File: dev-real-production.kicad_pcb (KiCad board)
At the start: 4 copper layers, 105 x 105 mm, 320 parts, among them IC1 ICM-42670-P, IC2 ENS161-BLGT_LGA9_T&R_1k5, J1 VIN_IN, J10 USB-C USB2 DEBUG, J11 ARM_JTAG_10, J12 SOP0_SELECT, J13 SOP1_SELECT, J14 Conn_01x03, J15 Conn_01x03, J16 ARM_JTAG_10, J17 USB-C Receptacle USB2, J18 Conn_01x03_Pin, J19 Cortex SWD/JTAG, J2 TP_EN_PG, J20 USB-C USB2 DEVICE, J21 HR911105A MAGJACK, J22 Conn_02x10_Counter_Clockwise, J23 Conn_02x04_Odd_Even, J3 TP_SW_FB, J4 USB-C Receptacle USB2, J5 Conn_01x03_Pin, J6 ARM_Cortex_Debug_10, J7 SMA_ANT_50OHM, J8 3V3_IN, U1 MMC5633NJL, U10 USBLC6-2P6, U11 FT230XS-R, U12 FT230XS-R, U13 IWRL6432BDBAAMFR, U14 MX25R1635FZUIH0, U15 MX25R1635FZUIH0, U16 AMS1117-1.8, U17 THS8136, U18 MM8108-MF15457, U19 AP2112K-1.8, U2 LPS22HH, U20 PGA113AIDGSR, U21 AD9609BCPZRL7-80, U22 MCP6D11T-E/MS, U23 STM32H7S3Z8T6, U24 LAN8742A-CZ-TR, U25 USBLC6-2SC6, U3 MIC28516T-E/PHA, U4 RP2350B, U5 XCC1352R1F3RGZR, U6 XMSSJJ3G0PA-054, U7 TLV75518PDBV, U8 TLV75518PDBVR, U9 USBLC6-2P6, Y1 12MHz ABM8-272-T3, Y2 48MHz, Y3 40MHz, Y4 40MHz, Y5 24MHz, Y6 32.768kHz, Y7 25MHz

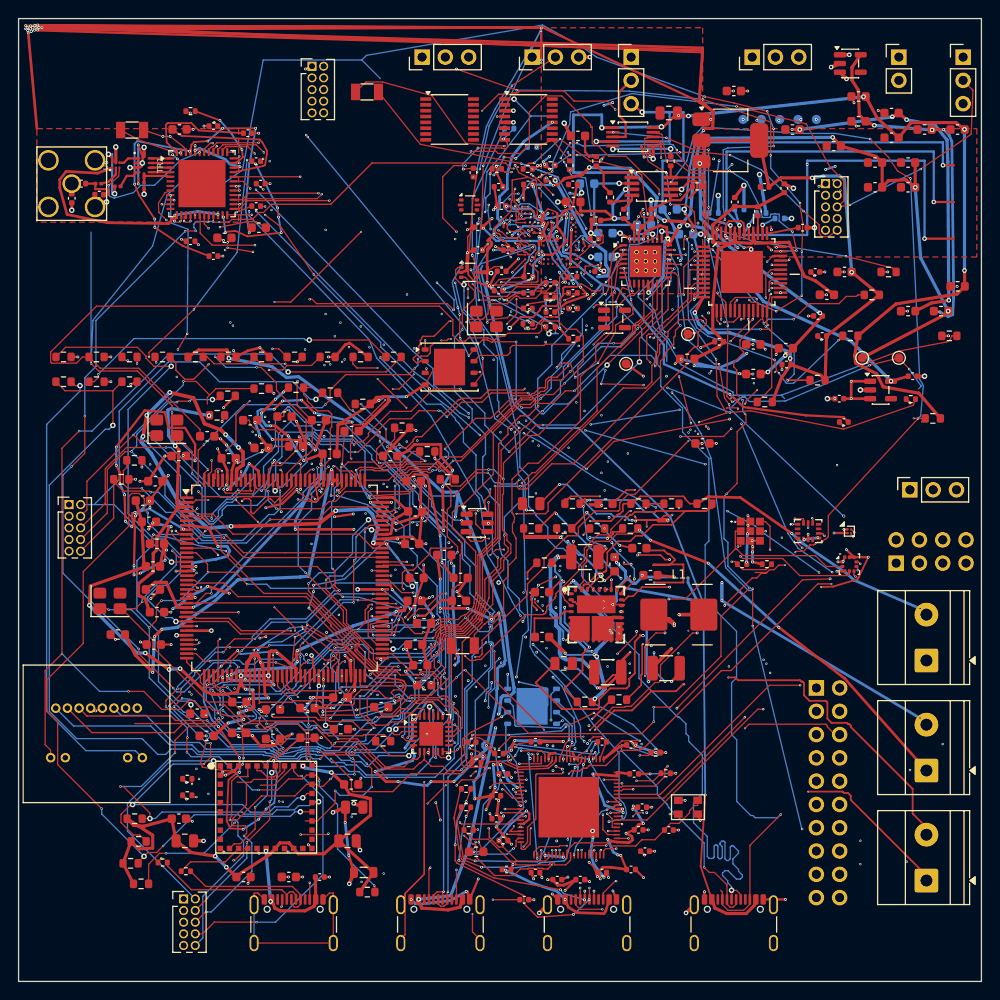
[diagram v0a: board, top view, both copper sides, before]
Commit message: route: update manual pair tuning candidate
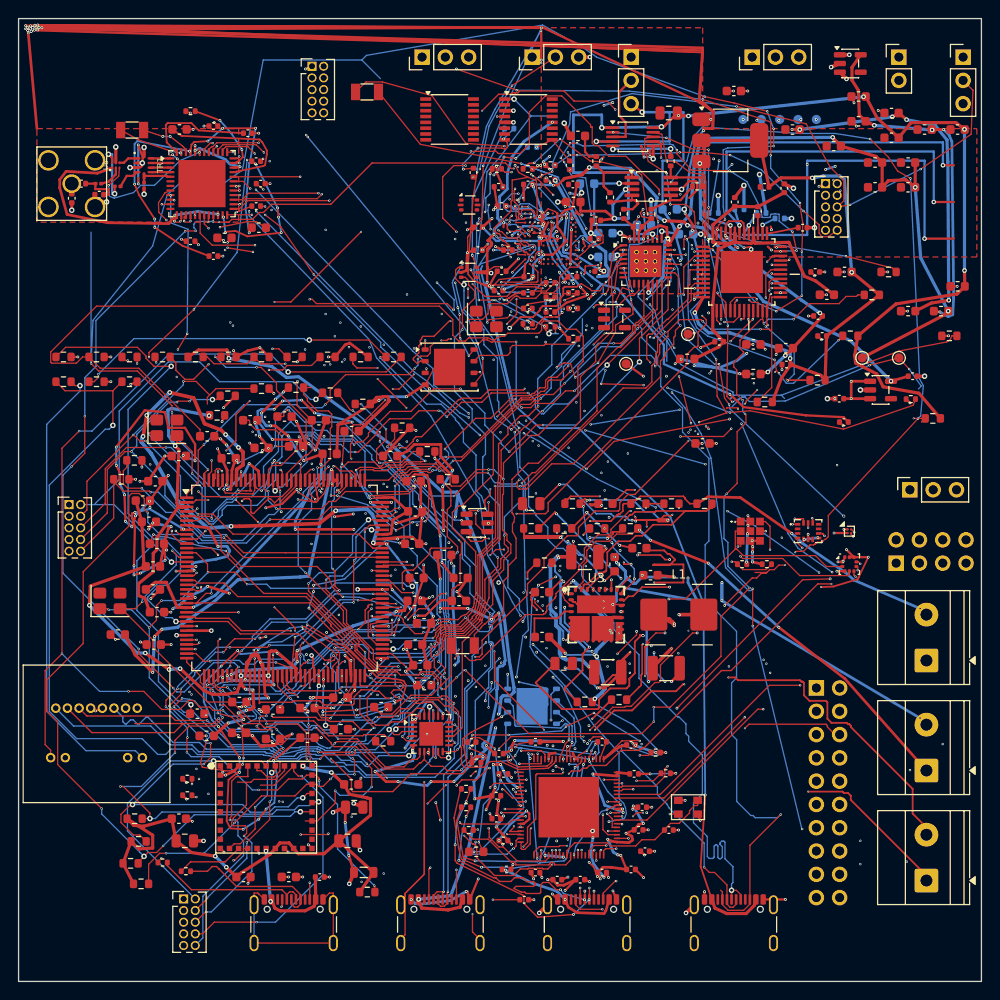
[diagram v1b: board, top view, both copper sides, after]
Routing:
- net /IWRL6432BD/USB_DP_CONN: track 100.6 -> 92.7 mm
- net /RP2350/USB_D_P_CONN: track 23.4 -> 30.3 mm
- net /AD9609/MCP_OUT_P: track 4.25 -> 5.70 mm
- net /STM32H7/PHY_RXN: track 41.3 -> 42.6 mm

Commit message: route: refine STM32 USB pair matching
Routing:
- net /MM8108/ANT: track 0.00 -> 24.9 mm
- net /MM8108/JTAG_TDI: track 34.5 -> 30.0 mm
- net /MM8108/JTAG_TMS: track 30.7 -> 33.9 mm
- net GND: track 1682.8 -> 1680.5 mm
- net /STM32H7/USB_CONN_DP: track 45.8 -> 47.5 mm
- net /MM8108/SDIO_CLK_SPI_SCK: track 56.8 -> 56.1 mm
